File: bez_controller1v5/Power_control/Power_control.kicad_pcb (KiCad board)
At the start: 2 copper layers, 40 x 35 mm, 7 parts, among them J1 Screw_Terminal_01x02, Q2 IRF4905STRLPBF, SW1 GPB040B05BR

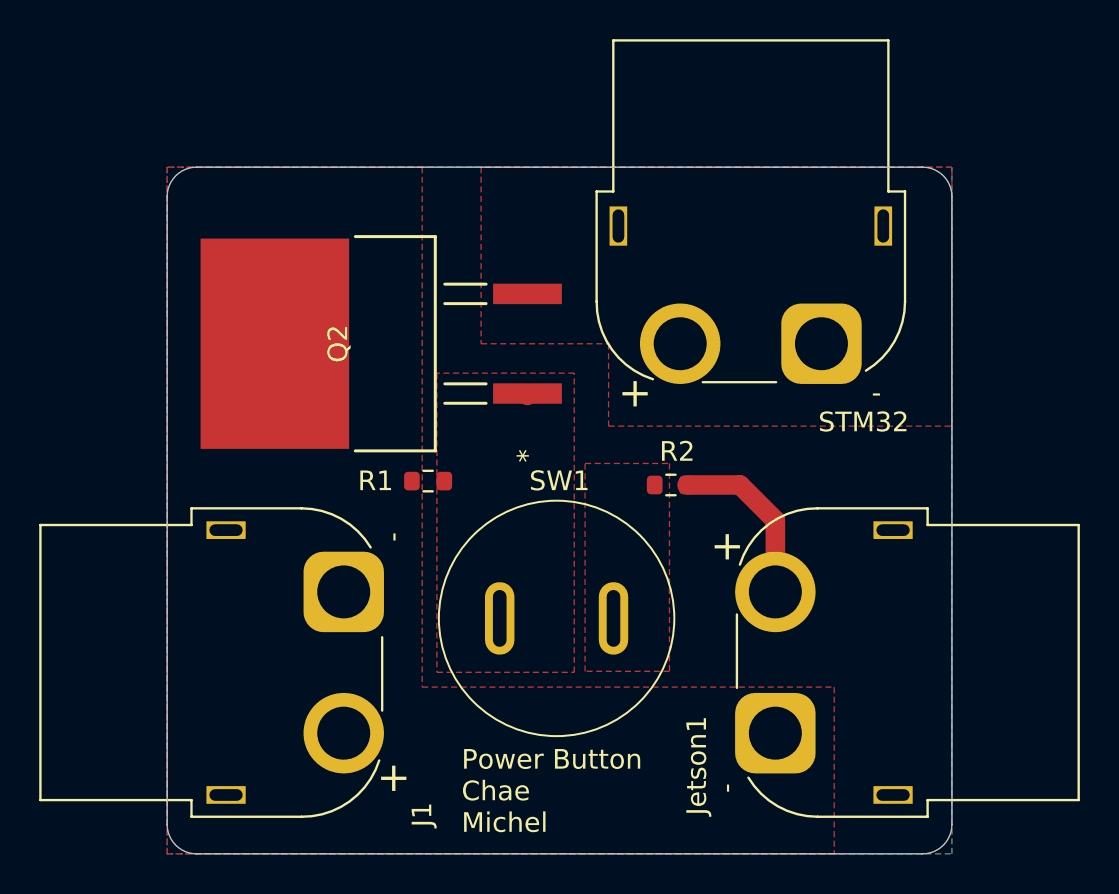
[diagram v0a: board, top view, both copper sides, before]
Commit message: Fixed XT60 polarity
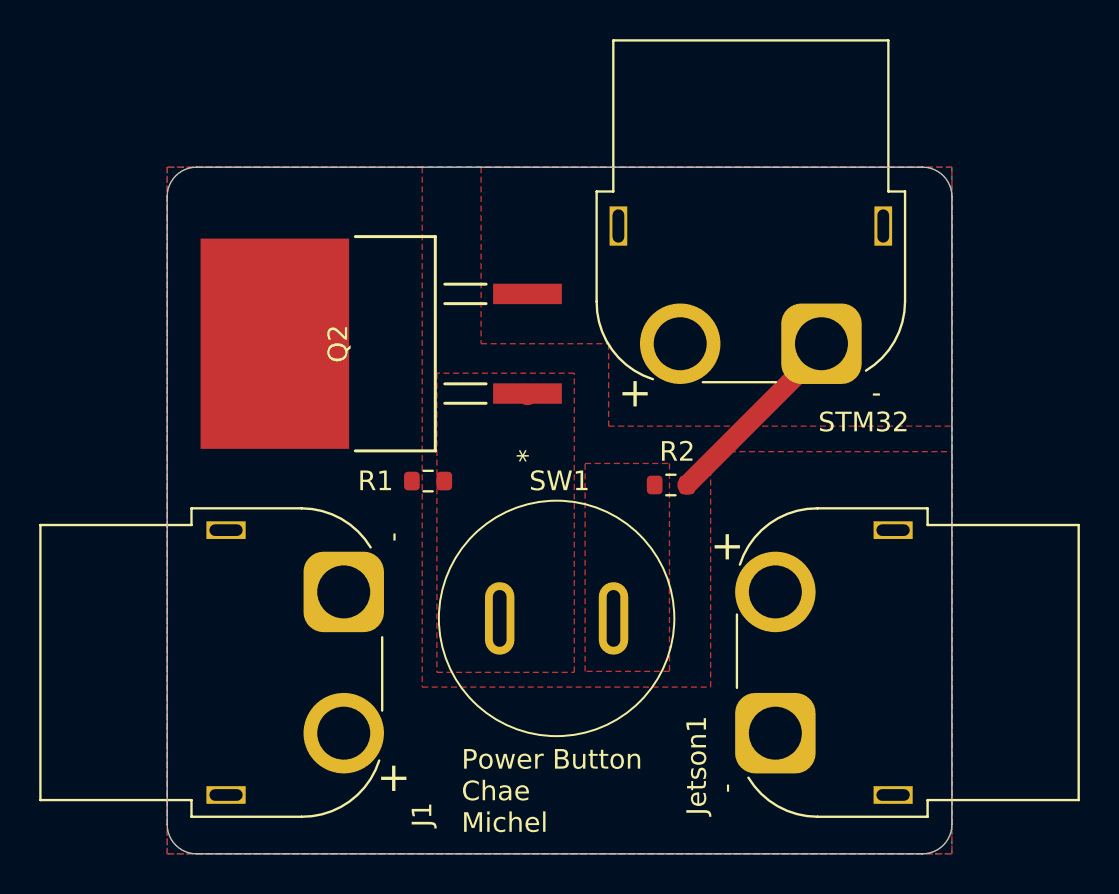
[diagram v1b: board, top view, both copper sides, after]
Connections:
- J1 pad 1: +12V -> GND
- J1 pad 2: GND -> +12V
- Jetson1 pad 1: +12V -> GND
- Jetson1 pad 2: GND -> +12V
- Q2 pad 2: Net-(STM32-Pin_1) -> Net-(STM32-Pin_2)
- STM32 pad 1: Net-(STM32-Pin_1) -> GND
- STM32 pad 2: GND -> Net-(STM32-Pin_2)
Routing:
- net GND: track 8.90 -> 10.0 mm
- added copper zone on F.Cu, net Net-(STM32-Pin_2)
- removed copper zone on F.Cu, net Net-(STM32-Pin_1)
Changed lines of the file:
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@@
 	(net 2 "+12V")
 	(net 3 "Net-(Q2-Pad1)")
-	(net 4 "Net-(STM32-Pin_1)")
+	(net 4 "Net-(STM32-Pin_2)")
 	(net 5 "Net-(R2-Pad1)")
 	(footprint "Resistor_SMD:R_0603_1608Metric"
@@
 		(tags "resistor")
 		(property "Reference" "R1"
-			(at -2.675 0 360)
+			(at -2.675 0 0)
 			(layer "F.SilkS")
 			(effects
@@
 		)
 		(property "Value" "10k"
-			(at 0 1.43 360)
+			(at 0 1.43 0)
 			(layer "F.Fab")
 			(hide yes)
@@
 		)
 		(fp_text user "${REFERENCE}"
-			(at 0 0 360)
+			(at 0 0 0)
 			(layer "F.Fab")
 			(effects
@@
 		(tags "resistor")
 		(property "Reference" "R2"
-			(at 0.325 -1.7 360)
+			(at 0.325 -1.7 0)
 			(layer "F.SilkS")
 			(effects
@@
 		)
 		(property "Value" "10k"
-			(at 0 1.43 360)
+			(at 0 1.43 0)
 			(layer "F.Fab")
 			(hide yes)
@@
 		)
 		(fp_text user "${REFERENCE}"
-			(at 0 0 360)
+			(at 0 0 0)
 			(layer "F.Fab")
 			(effects
@@
 			(size 1.0414 3.5052)
 			(layers "F.Cu" "F.Paste" "F.Mask")
-			(net 4 "Net-(STM32-Pin_1)")
+			(net 4 "Net-(STM32-Pin_2)")
 			(pinfunction "2")
 			(pintype "unspecified")
@@
 			(remove_unused_layers no)
 			(roundrect_rratio 0.25)
-			(net 2 "+12V")
+			(net 1 "GND")
 			(pinfunction "Pin_1")
 			(pintype "passive")
@@
 			(layers "*.Cu" "*.Mask")
 			(remove_unused_layers no)
-			(net 1 "GND")
+			(net 2 "+12V")
 			(pinfunction "Pin_2")
 			(pintype "passive")
@@
 			(remove_unused_layers no)
 			(roundrect_rratio 0.25)
-			(net 4 "Net-(STM32-Pin_1)")
+			(net 1 "GND")
 			(pinfunction "Pin_1")
 			(pintype "passive")
@@
 			(layers "*.Cu" "*.Mask")
 			(remove_unused_layers no)
-			(net 1 "GND")
+			(net 4 "Net-(STM32-Pin_2)")
 			(pinfunction "Pin_2")
 			(pintype "passive")
@@
 			(remove_unused_layers no)
 			(roundrect_rratio 0.25)
-			(net 2 "+12V")
+			(net 1 "GND")
 			(pinfunction "Pin_1")
 			(pintype "passive")
@@
 			(layers "*.Cu" "*.Mask")
 			(remove_unused_layers no)
-			(net 1 "GND")
+			(net 2 "+12V")
 			(pinfunction "Pin_2")
 			(pintype "passive")
@@
 	)
 	(segment
-		(start 180 70)
-		(end 180 73.65)
+		(start 182.35 61.35)
+		(end 182.35 61)
 		(width 1)
 		(layer "F.Cu")
@@
 	(segment
 		(start 175.5 68.2)
-		(end 178.2 68.2)
-		(width 1)
-		(layer "F.Cu")
-		(net 1)
-	)
-	(segment
-		(start 178.2 68.2)
-		(end 180 70)
+		(end 182.35 61.35)
 		(width 1)
 		(layer "F.Cu")
@@
 	(zone
 		(net 4)
-		(net_name "Net-(STM32-Pin_1)")
+		(net_name "Net-(STM32-Pin_2)")
 		(layer "F.Cu")
 		(hatch edge 0.5)
@@
 		(polygon
 			(pts
-				(xy 162 78.5) (xy 183 78.5) (xy 183 87) (xy 149 87) (xy 149 52) (xy 162 52)
-			)
-		)
+				(xy 162 78.5) (xy 176.7 78.5) (xy 176.7 66.5) (xy 189 66.5) (xy 189 87) (xy 149 87) (xy 149 52)
+				(xy 162 52)
+			)
+		)

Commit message: Fixed Drain and Source
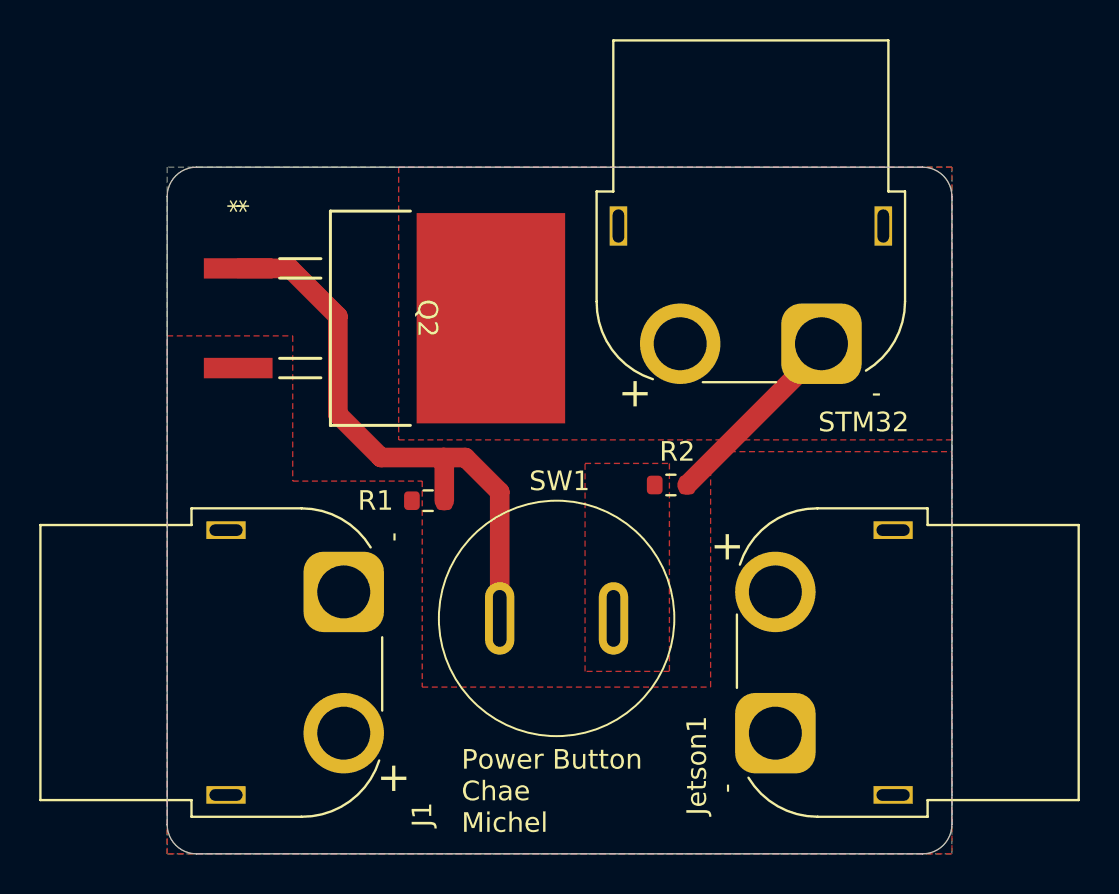
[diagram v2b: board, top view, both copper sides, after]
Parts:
- moved Q2 4.74 mm to (162.3, 59.7), turned to -90 degrees
- moved R1 1.00 mm to (162.3, 69.0)
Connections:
- Q2 pad 2: Net-(STM32-Pin_2) -> +12V
- Q2 pad 3: +12V -> Net-(STM32-Pin_2)
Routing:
- net Net-(Q2-Pad1): track 0.09 -> 29.6 mm
- removed copper zone on F.Cu, net Net-(Q2-Pad1)

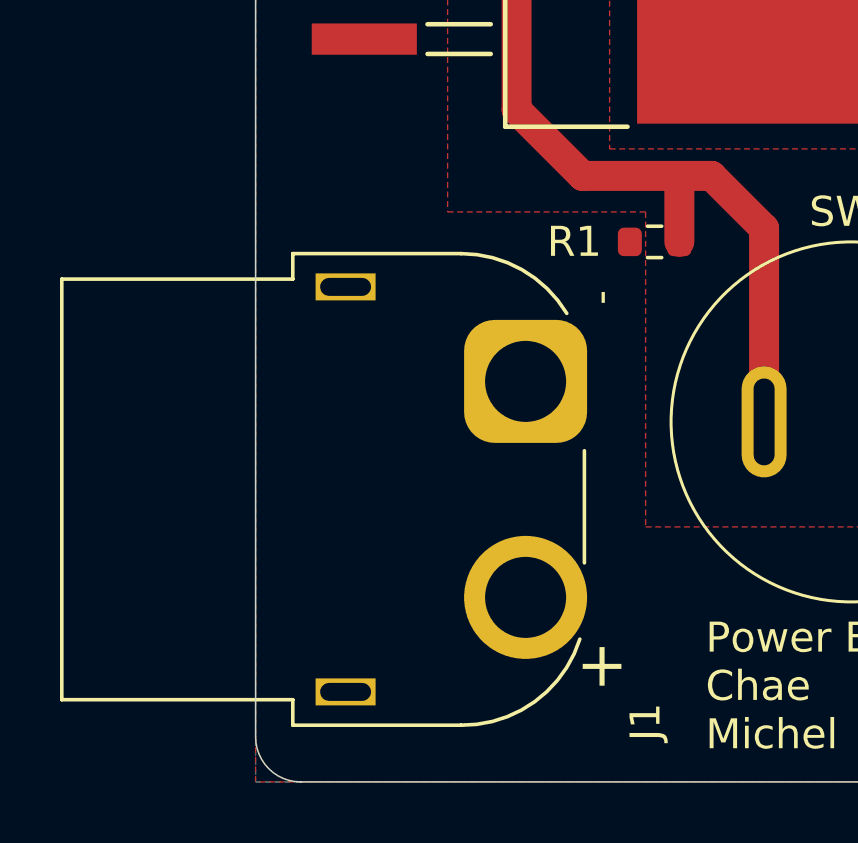
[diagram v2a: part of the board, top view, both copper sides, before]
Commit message: changed battery side XT60 into a vertical one
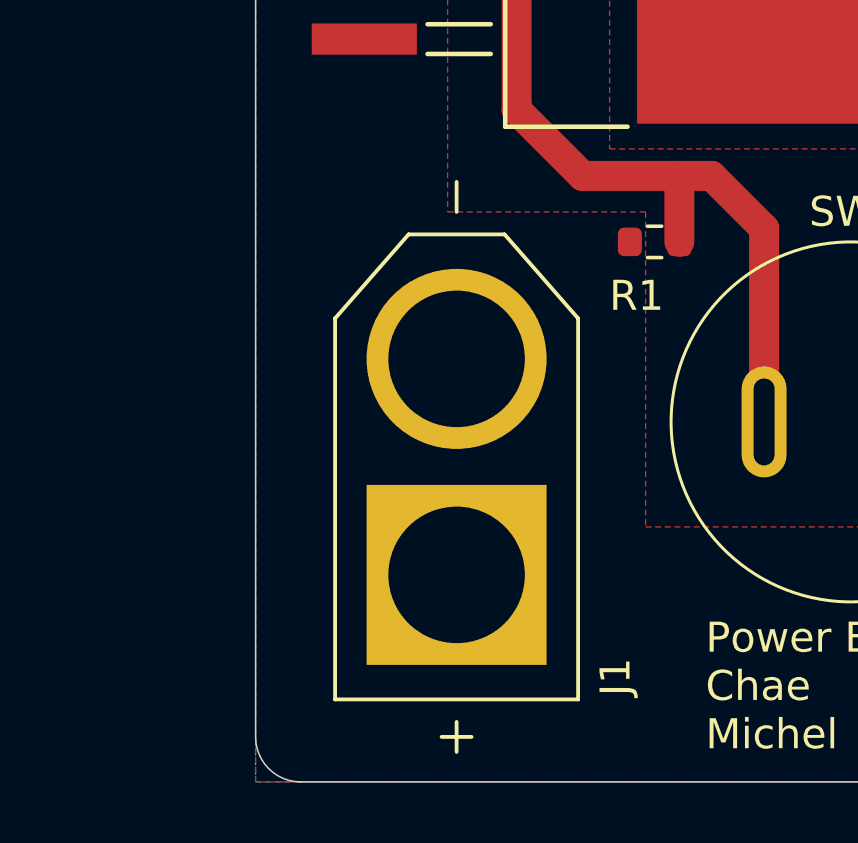
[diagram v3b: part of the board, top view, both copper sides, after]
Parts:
- J1: footprint Connector_AMASS:AMASS_XT60PW-F_1x02_P7.20mm_Horizontal -> xt60:AMASS_XT60-M
- moved J1 3.66 mm to (155.7, 76.5)
